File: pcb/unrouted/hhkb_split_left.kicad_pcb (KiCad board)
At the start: 2 copper layers, 140.4 x 97.4 mm, 65 parts, among them SW1 CPG151101S11-2, SW10 CPG151101S11-2, SW11 CPG151101S11-2, SW12 CPG151101S11-2, SW13 CPG151101S11-2, SW14 CPG151101S11-2, SW15 CPG151101S11-2, SW16 CPG151101S11-2, SW17 CPG151101S11-2, SW18 CPG151101S11-2, SW19 CPG151101S11-2, SW2 CPG151101S11-2, SW20 CPG151101S11-2, SW21 CPG151101S11-2, SW22 CPG151101S11-2, SW23 CPG151101S11-2, SW24 CPG151101S11-2, SW25 CPG151101S11-2, SW26 CPG151101S11-2, SW27 CPG151101S11-2, SW3 CPG151101S11-2, SW4 CPG151101S11-2, SW5 CPG151101S11-2, SW6 CPG151101S11-2, SW7 CPG151101S11-2, SW8 CPG151101S11-2, SW9 CPG151101S11-2, U1 74LVC595

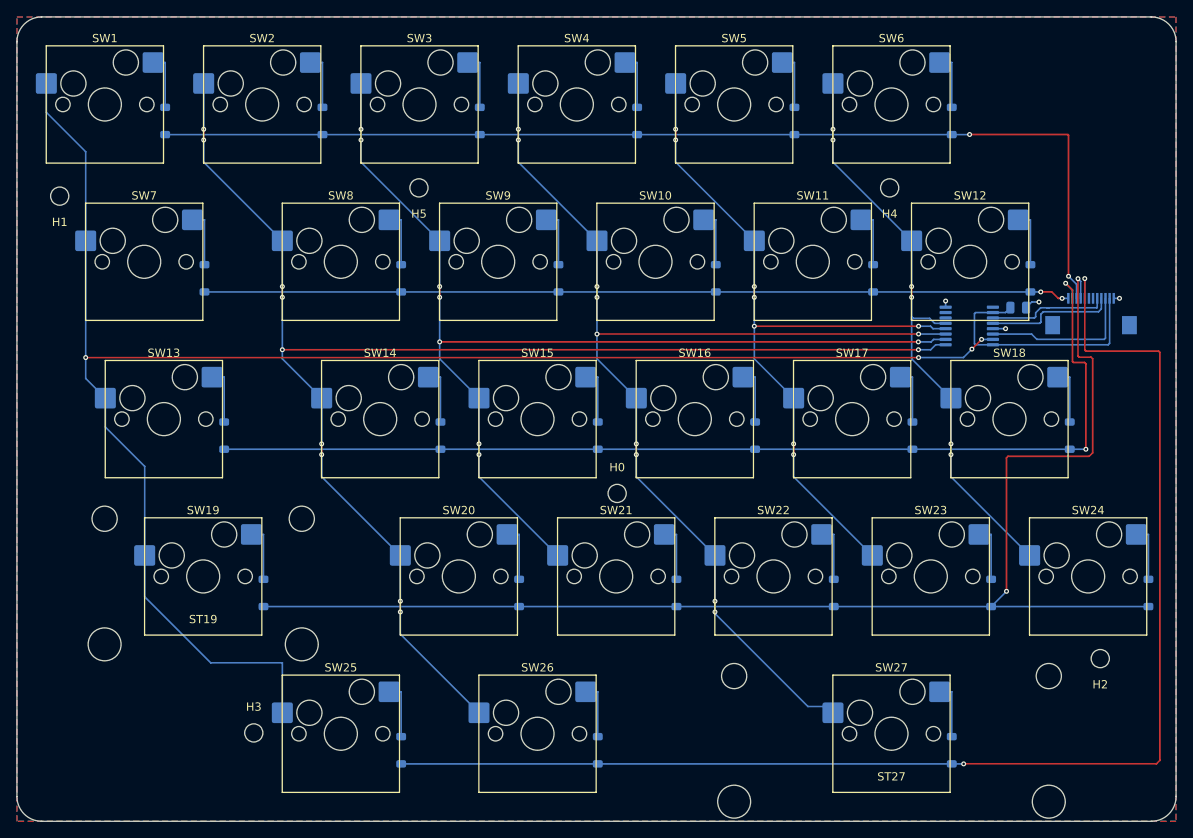
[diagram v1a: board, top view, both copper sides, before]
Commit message: #51 の基板一式——3 枚とも DRC 違反 0 / 未配線 0
利用者が右の J_DB 周り 9 ネットを新しい位置へ引き直し（matrix_only）、
V3V3 の切れ目と、写しの φ0.5→0.56 化で近すぎたビア 3 ペアも修正。
写し（matrix_routing.json）→ gen_pcb（外形 左 138.4 / 右 171.7）→
finalize --src unrouted → DRC の全経路を通した。部品位置の写しを含む。

Co-Authored-By: Claude Fable 5 <noreply@anthropic.com>
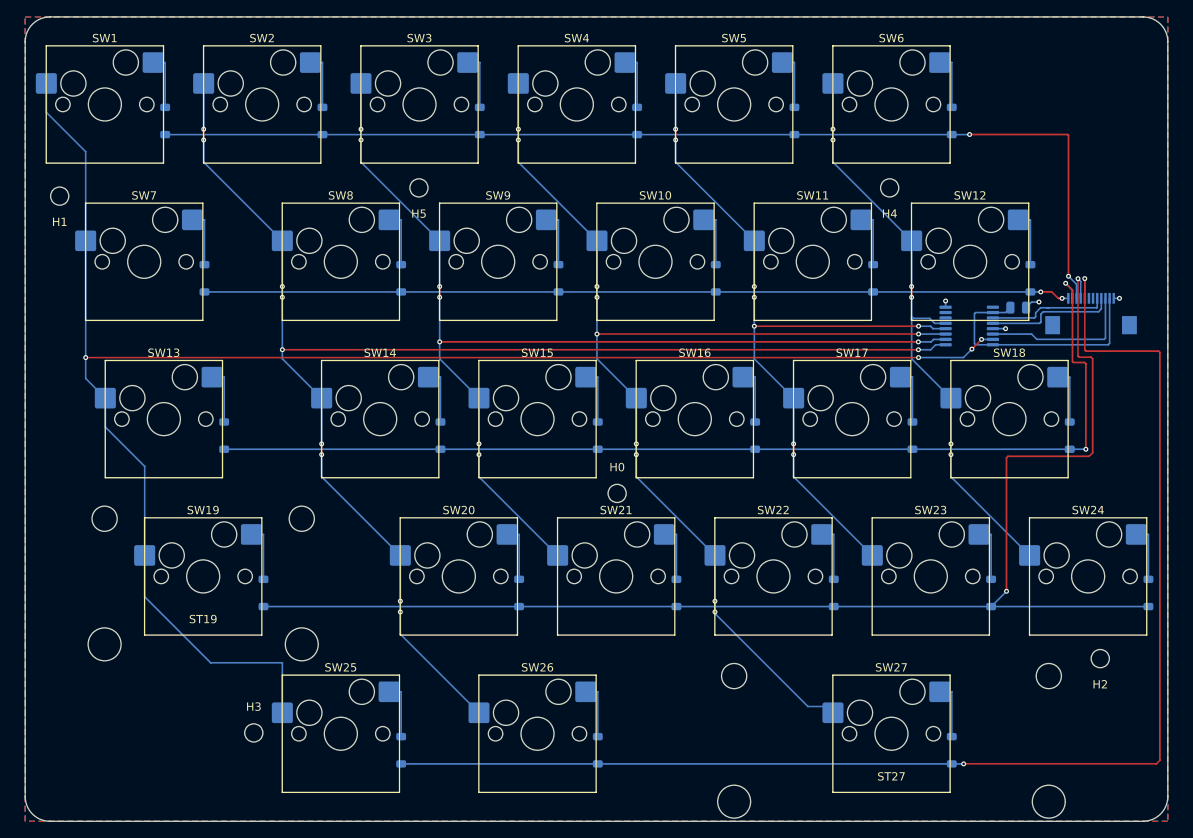
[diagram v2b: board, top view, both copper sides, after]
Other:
- board size 140.4 x 97.4 mm -> 138.4 x 97.4 mm

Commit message: #49 オシロ用テストパッドを実装した（左 5・右 6・実装なしのランド）
利用者の決定（Yes）。信号は SPI_SCK / SPI_MOSI / CS / V3V3 / GND、右は
595 の数珠つなぎ U1_U2 も。ROW/COL はダイオードとソケットのパッドで
見られるので出さない。kind `testpoint` を回路宣言・pinmap・
parts.NOT_ASSEMBLED（BOM/CPL に出さない）・回路図の群・gen_pcb の
絶対座標配置（TP_PLACE・本番の板の空きを実測して決めた）に通した。

検査側の修正: TestPoint 系フットプリントの円コートヤードを
_courtyard_bbox が読めず「コートヤード無し」と誤判定していた（四角を
足したら自己交差になって発覚）→ fp_circle も読む。

残り: 各パッドから既存ネットへのスタブ（GND 以外）を利用者が引く
（左 4・右 5）。引くまで DRC の未配線がその本数ぶん残る。

Co-Authored-By: Claude Fable 5 <noreply@anthropic.com>
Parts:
- added TP1: testpoint, TestPoint_Pad_D1.5mm, B.Cu at (200.0, 71.6)
- added TP2: testpoint, TestPoint_Pad_D1.5mm, B.Cu at (202.5, 71.6)
- added TP3: testpoint, TestPoint_Pad_D1.5mm, B.Cu at (205.1, 71.6)
- added TP4: testpoint, TestPoint_Pad_D1.5mm, B.Cu at (207.6, 71.6)
- added TP5: testpoint, TestPoint_Pad_D1.5mm, B.Cu at (210.2, 71.6)

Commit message: Revert "#49 オシロ用テストパッドを実装した"——利用者が取り消しを決定
パッドから既存ネットへのスタブが引けず（利用者「試行錯誤したが諦める」）。
代案（利用者提案）: 既存のビアのレジストを剥がしてリード線を半田付けできる
ようにする。部品追加も配線も不要。別コミットで実装する。
検査側の修正（_courtyard_bbox が fp_circle も読む）だけは有用なので残す。

This reverts commits b8ea548 and 4f7bba2 (except the test improvement).

Co-Authored-By: Claude Fable 5 <noreply@anthropic.com>
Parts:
- removed TP1, TP2, TP3, TP4, TP5: testpoint, TestPoint_Pad_D1.5mm

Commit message: #49 露出規則の「部品本体」を Fab 外形に統一し、利用者の左ビア 2 個を取り込んだ——全ネット露出・検査緑
- ソケットに bands.SOCK_*（ケース側の帯）、電子部品にコートヤードを使っていて
  届くビア（右 U1_U2・左 SPI_SCK/V3V3）を弾いていた。実物の外形（Fab 図形）へ
- 左右とも 5 ネット + GND を露出。DRC 3 枚 違反 0（左 +2 は利用者ビアの via_dangling）
- 部品記録・DRC 記録・open-gaps #49・記録資料 項目 25 を更新

Co-Authored-By: Claude Fable 5 <noreply@anthropic.com>
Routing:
- net V3V3: track 30.2 -> 31.9 mm, vias 0 -> 1
- net SPI_SCK: track 14.5 -> 16.2 mm, vias 0 -> 1

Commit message: #49 左 SPI_MOSI / CS にも利用者のビア——左右 5+5 ネットを全部ビアで露出（配線の窓なし）
- DRC 3 枚 違反 0（左 +2 は新ビアの via_dangling）・test_pcb 79 緑
- 部品記録・DRC 記録・open-gaps #49・記録資料 項目 25 を更新

Co-Authored-By: Claude Fable 5 <noreply@anthropic.com>
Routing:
- net CS: track 15.7 -> 18.3 mm, vias 0 -> 1
- net SPI_MOSI: vias 0 -> 1

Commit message: #19 J_DB の口を奥向きに回した（FFC は直線・A タイプで正しい）。左は配線無傷で DRC 0、右は J_DB 周りの引き直し待ち
- 原因: 2026-08-08 の初回配置で Flip() の副作用の 180° をそのまま使い、誰も口の向きを決めていなかった（git 履歴で確認）
- circuit.py: J_DB のピン表を J_MAIN の鏡像（n ↔ 13-n）に。裏面で 180° 回すとピン 1 の側が入れ替わるため。検査 2 本と決定文書を鏡像に更新
- gen_pcb.py: J_DB に向き 0° と dy（左 -3.7 / 右 -0.4）。配置は matrix_only の現物が優先
- 左 matrix_only: J_DB を 0°・3.7mm 奥へ → 12 パッドが同じ座標に戻り配線無傷。DRC 0/0
- 右 matrix_only: 3.7mm は SW10 の NPTH がコートヤードに入るため 0.4mm 止まり。パッドが南側の枝と重なり DRC 違反 20・未配線 8（利用者の引き直し・open-gaps #19 に手順）
- gen_assembly.py: 幕と床走行を消し、口の直後の潜り＋J_MAIN までの斜めのリボンに。箱モード干渉 0
- 回路図・部品記録・DRC 記録・証拠ページを更新。検査 455 緑・5 赤（全部右の引き直しと露出ビアの打ち直しに帰着・open-gaps に列挙）

Co-Authored-By: Claude Fable 5 <noreply@anthropic.com>
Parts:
- moved J_DB 3.70 mm to (209.9, 83.5), turned to 0 degrees
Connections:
- J_DB pad 1: GND -> ROW_E
- J_DB pad 10: ROW_C -> SPI_MOSI
- J_DB pad 11: ROW_D -> V3V3
- J_DB pad 12: ROW_E -> GND
- J_DB pad 2: V3V3 -> ROW_D
- J_DB pad 3: SPI_MOSI -> ROW_C
- J_DB pad 4: CS -> ROW_B
- J_DB pad 5: SPI_SCK -> ROW_A
- J_DB pad 6: SPARE2 -> SPARE
- J_DB pad 7: SPARE -> SPARE2
- J_DB pad 8: ROW_A -> SPI_SCK
- J_DB pad 9: ROW_B -> CS
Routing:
- net SPARE2: track 0.00 -> 4.48 mm, vias 0 -> 1
- net SPARE: track 0.00 -> 4.03 mm, vias 0 -> 1
- net SPI_SCK: track 16.2 -> 18.4 mm
